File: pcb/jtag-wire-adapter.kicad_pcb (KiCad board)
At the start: 2 copper layers, 21.6 x 27.9 mm, 3 parts, among them J1 Conn_02x10_Odd_Even, J2 Conn_01x07_Pin

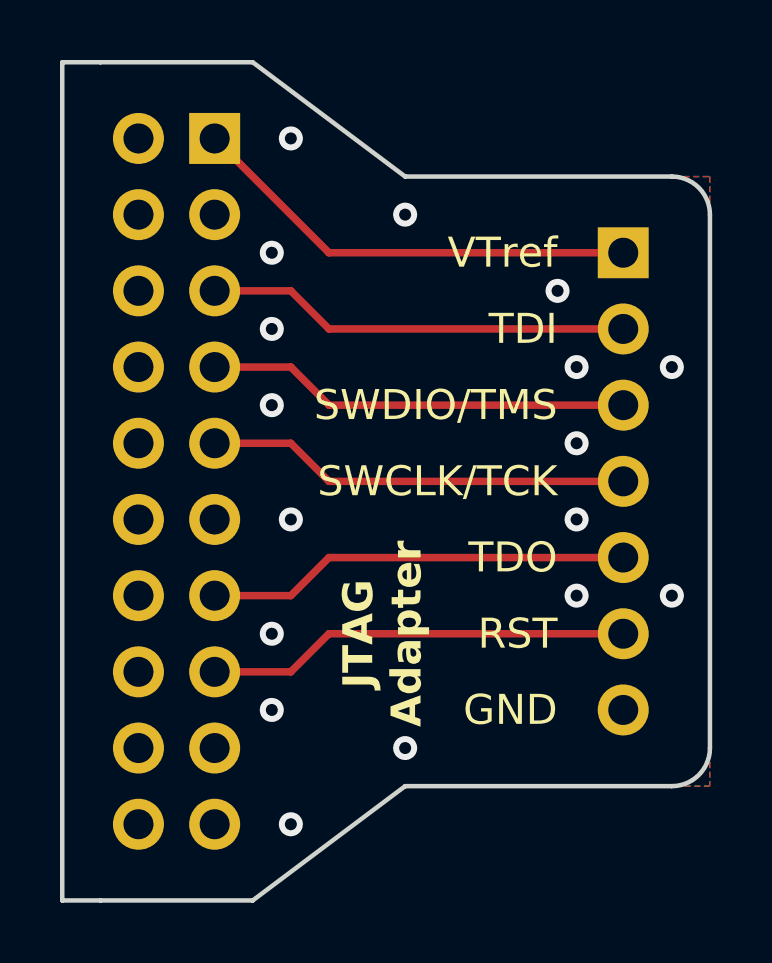
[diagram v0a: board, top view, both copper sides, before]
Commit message: Adjusted DRC, layout for prototyping
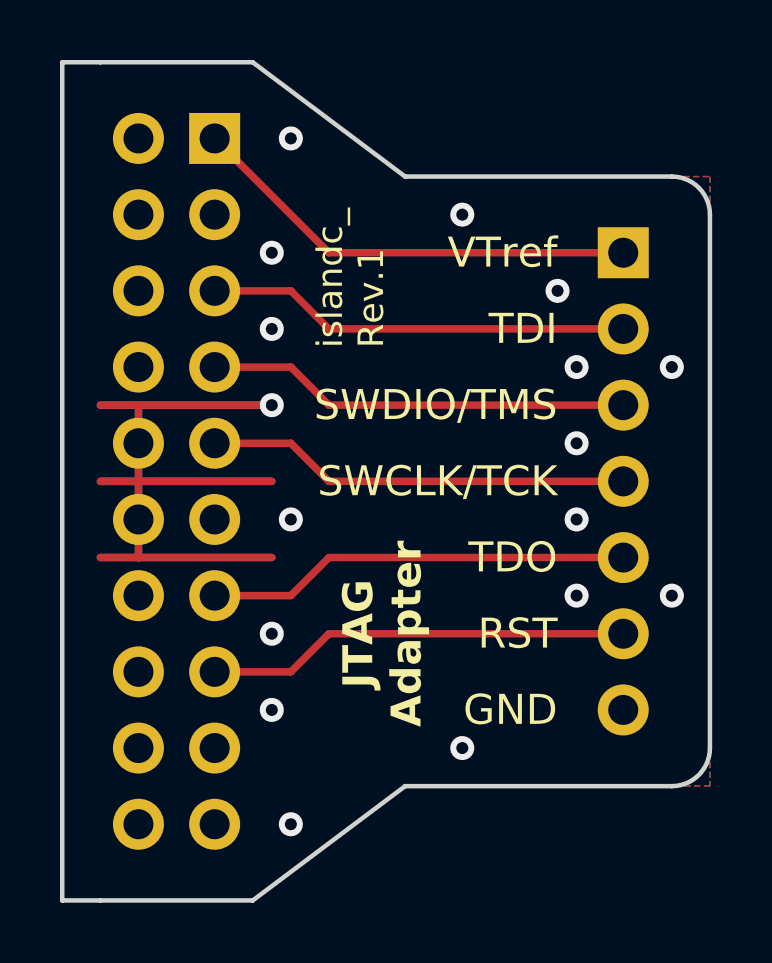
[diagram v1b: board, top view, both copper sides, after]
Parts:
- removed REF**: CE-Logo_8.5x6mm_SilkScreen, Symbol:CE-Logo_8.5x6mm_SilkScreen
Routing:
- net GND: track 0.00 -> 44.5 mm
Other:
- board text added: "islandc_ Rev.${REVISION}"
- board text removed: "islandc_ 2023"

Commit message: Added SWO label
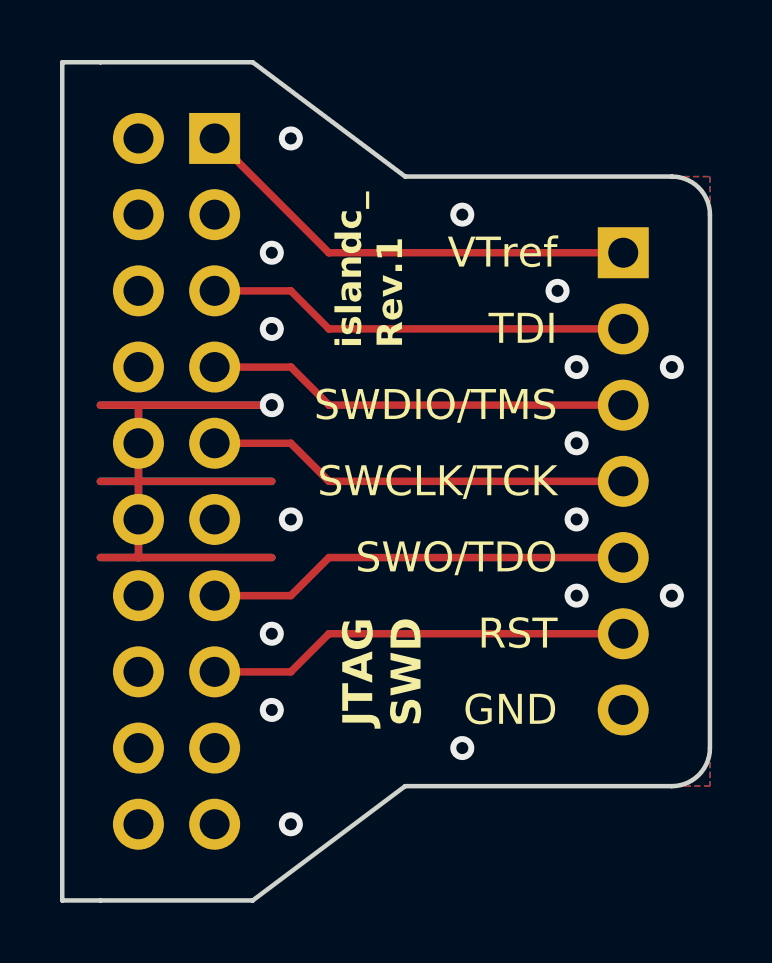
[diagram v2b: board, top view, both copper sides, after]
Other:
- board text added: "JTAG SWD"
- board text added: "SWO/TDO"
- board text removed: "JTAG Adapter"
- board text removed: "TDO"
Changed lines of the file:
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@@
     (effects (font (size 1 1) (thickness 0.15)) (justify right))
   )
-  (gr_text "TDO" (at 143.51 107.95) (layer "F.SilkS")
+  (gr_text "SWO/TDO" (at 143.51 107.95) (layer "F.SilkS")
     (effects (font (size 1 1) (thickness 0.15)) (justify right))
   )
@@
     (effects (font (size 1 1) (thickness 0.15)) (justify right))
   )
-  (gr_text "JTAG\nAdapter" (at 139.065 110.49 90) (layer "F.SilkS" knockout)
+  (gr_text "JTAG\nSWD" (at 139.065 111.76 90) (layer "F.SilkS" knockout)
     (effects (font (size 1 1) (thickness 0.25) bold) (justify bottom))
   )
@@
     (effects (font (size 1 1) (thickness 0.15)) (justify right))
   )
-  (gr_text "islandc_\nRev.${REVISION}" (at 137.795 100.965 90) (layer "F.SilkS")
-    (effects (font (size 0.85 0.85) (thickness 0.15)) (justify left bottom))
+  (gr_text "islandc_\nRev.${REVISION}" (at 138.43 100.965 90) (layer "F.SilkS")
+    (effects (font (size 0.85 0.85) (thickness 0.2) bold) (justify left bottom))
   )
   (segment (start 135.89 97.79) (end 132.08 93.98) (width 0.25) (layer "F.Cu") (net 1))
